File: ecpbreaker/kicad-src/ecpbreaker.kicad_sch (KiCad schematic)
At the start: 49 parts, among them J24 USB_C_Receptacle_USB2.0, SW1 TACT, U1 TPD3S014, U10 LM3880MF-1AF, U2 CY7C68013A-56LTX, U7 CAT24C256W, U8 ECP5U-12-CABGA256, Y1 24M

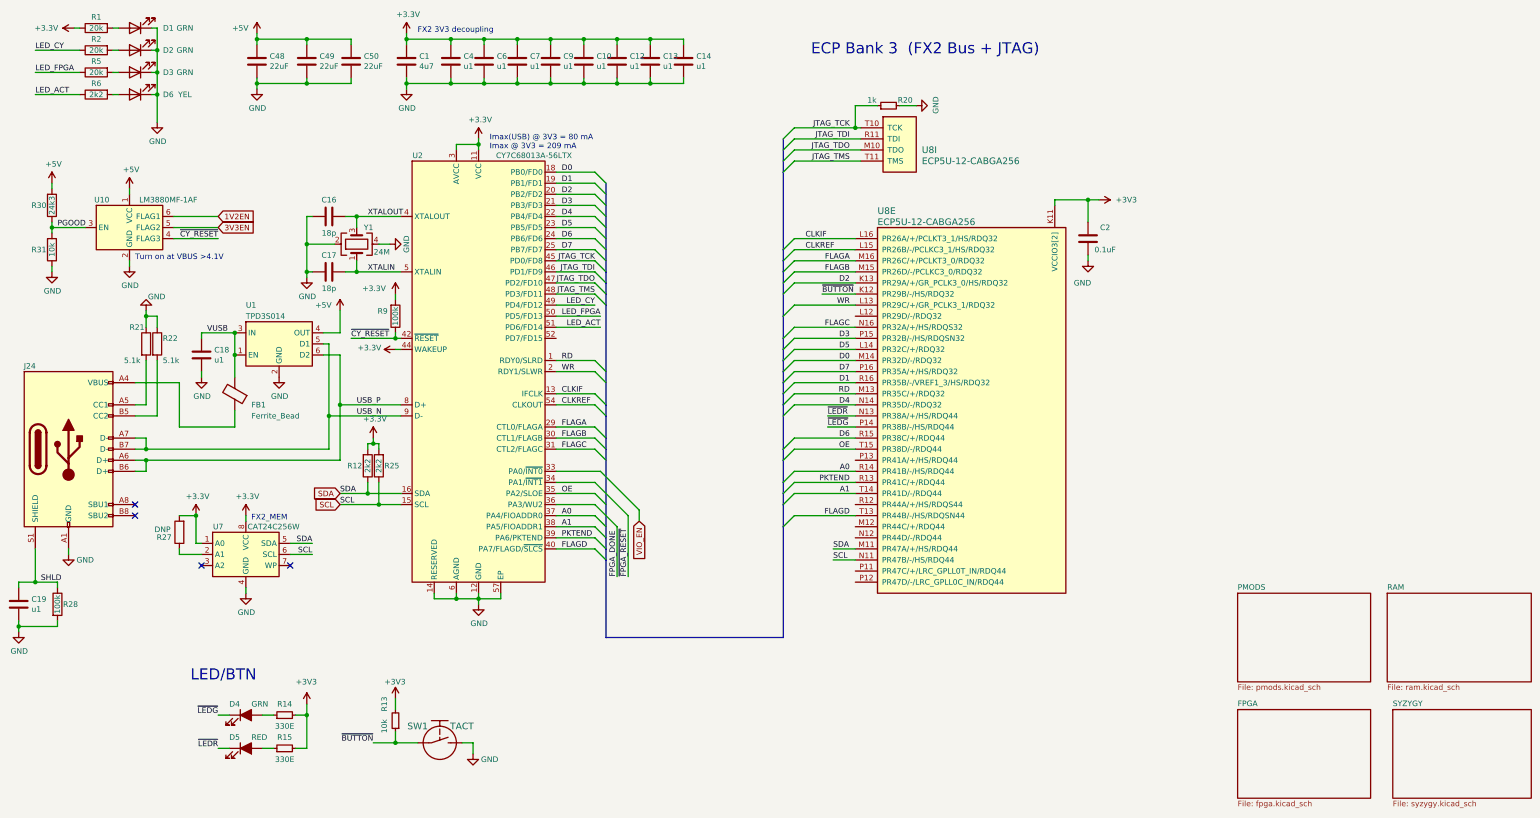
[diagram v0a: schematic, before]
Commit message: ecpbreaker: Add BOM values to project
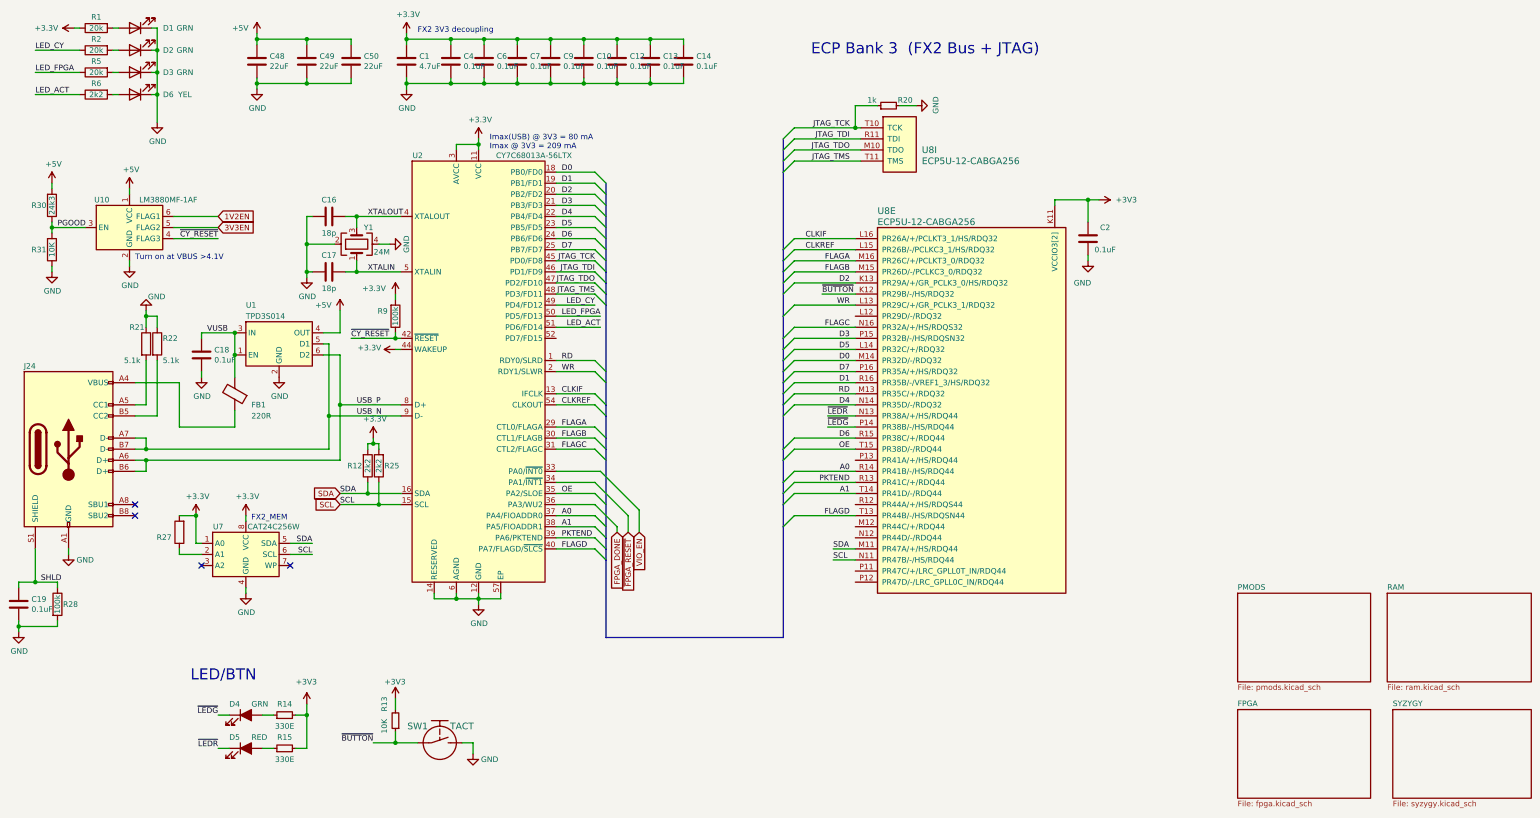
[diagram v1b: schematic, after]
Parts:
- C1: value 4u7 -> 4.7uF; 1b2-bom-key cap-cer-0603-4u7 -> (none); MPN LMK107BJ475KAHT -> (none); Mfg Taiyo Yuden -> Yageo; PN (none) -> CC0603KRX5R6BB475
- C10, C12, C13, C14, C18, C19, C4, C6, C7, C9: value u1 -> 0.1uF; 1b2-bom-key cap-cer-0402-100n -> (none); MPN TMK105BJ104KV-F -> (none); Mfg Taiyo Yuden -> Yageo; PN (none) -> CC0402JRX7R7BB104
- C16, C17: 1b2-bom-key cap-cer-0402-18p -> (none); MPN CC0402JRNPO8BN180 -> (none); PN (none) -> CC0402JRNPO9BN180
- C2: Mfg (none) -> Yageo; PN (none) -> CC0402JRX7R7BB104
- C48: 1b2-bom-key cap-cer-0603-4u7 -> (none); MPN LMK107BJ475KAHT -> (none); Mfg Taiyo Yuden -> Samsung Electro-Mechanics; PN (none) -> CL10A226MP8NUNE
- C49, C50: 1b2-bom-key cap-cer-0402-100n -> (none); MPN TMK105BJ104KV-F -> (none); Mfg Taiyo Yuden -> Samsung Electro-Mechanics; PN (none) -> CL10A226MP8NUNE
- D1, D2, D3: 1b2-bom-key led-0603-grn -> (none); MPN 150060GS75000 -> (none); Mfg Wurth Electronics -> EKINGLUX; PN (none) -> E6C0603YGAC1UDA
- D4: Key led-0603-grn -> (none); Mfg (none) -> EKINGLUX; PN (none) -> E6C0603YGAC1UDA; Source ANY -> (none)
- D5: Key led-0603-red -> (none); Mfg (none) -> EKINGLUX; PN (none) -> E6C0603URAC1UDA; Source ANY -> (none)
- D6: 1b2-bom-key led-0603-yel -> (none); MPN 150060YS75000 -> (none); Mfg Wurth Electronics -> EKINGLUX; PN (none) -> E6C0603UYAC1UDA
- FB1: value Ferrite_Bead -> 220R; 1b2-bom-key ferrite-0402-600 -> (none); MPN BLM15PX601SZ1D -> (none); PN (none) -> BLM15AX221SN1D
- J24: Mfg (none) -> XKB Connectivity; PN (none) -> U262-161N-4BVC11
- R1, R2, R5: 1b2-bom-key res-0402-20k -> (none); MPN RC0402FR-1320KL -> (none); PN (none) -> AC0402FR-0720KL
- R12, R25, R6: 1b2-bom-key res-0402-2k2 -> (none); MPN RC0402FR-132K2L -> (none); PN (none) -> AC0402FR-072K2L
- R13: value 10k -> 10K; Key res-0402-10k -> (none); Mfg (none) -> Yageo; PN (none) -> AC0402FR-0710KL; Source ANY -> (none)
- R14, R15: Key res-0402-330 -> (none); Mfg (none) -> Yageo; PN (none) -> AC0402FR-07330RL; Source ANY -> (none)
- R20: Key res-0402-10k -> (none); Mfg (none) -> Yageo; PN (none) -> AC0402FR-071KL; Source ANY -> (none)
- R21, R22: Mfg (none) -> Yageo; PN (none) -> AC0402FR-075K1L
- R27: DNP DNP -> (none)
- R28, R9: 1b2-bom-key res-0402-100k -> (none); MPN RC0402FR-13100KL -> (none); PN (none) -> AC0402FR-07100KL
- R30: 1b2-bom-key res-0402-24k3 -> (none); MPN RC0402FR-1324K3L -> (none); PN (none) -> AC0402FR-0724K3L
- R31: value 10k -> 10K; 1b2-bom-key res-0402-10k -> (none); MPN RC0402FR-1310KL -> (none); PN (none) -> AC0402FR-0710KL
- SW1: Key sw-tact-top-3x4x25 -> (none); PN (none) -> PTS810SJK250SMTRLFS
- U1: 1b2-bom-key ic-sot23-6-tpd3s014 -> (none); MPN TPD3S014DBVR -> (none); PN (none) -> TPD3S014DBVR
- U10: 1b2-bom-key ic-sot23-6-lm3880mf-1af -> (none); MPN LM3880MFX-1AF/NOPB -> (none); PN (none) -> LM3880MF-1AA/NOPB
- U2: 1b2-bom-key ic-cy7c68013a-56ltx -> (none); MPN CY7C68013A-56LTXC -> (none); PN (none) -> CY7C68013A-56LTXC
- U7: 1b2-bom-key ic-soic8-cat24c256w -> (none); MPN CAT24C256WI-GT3 -> (none); PN (none) -> CAT24C256YI-GT3
- U8: PN (none) -> LFE5U-12F-7BG256I; manf# ECP5U_12 -> (none)
- Y1: 1b2-bom-key xtal-lfxtal-24mhz -> (none); MPN LFXTAL058124REEL -> (none); Mfg IQD -> TAITIEN Elec; PN (none) -> XXHBBCNAOF-24.000000MHZ
